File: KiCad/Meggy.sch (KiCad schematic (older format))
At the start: 2 parts, among them U1 ROM-42pin, U2 AT90USB1286-MU

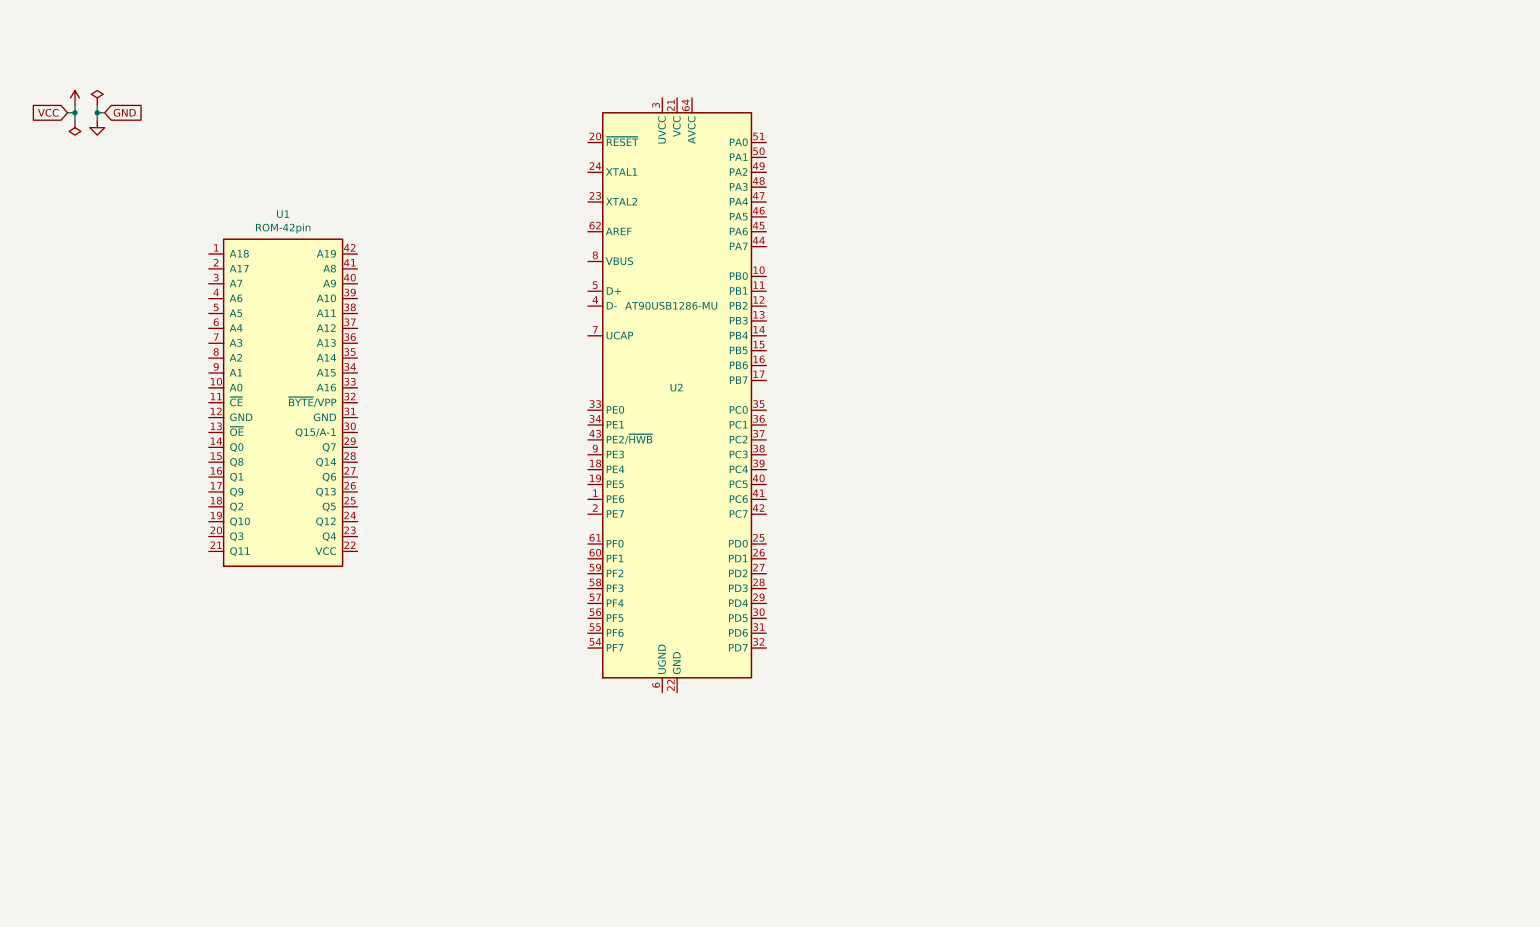
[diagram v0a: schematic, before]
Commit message: Add Micro USB connector and resistors R1-R3
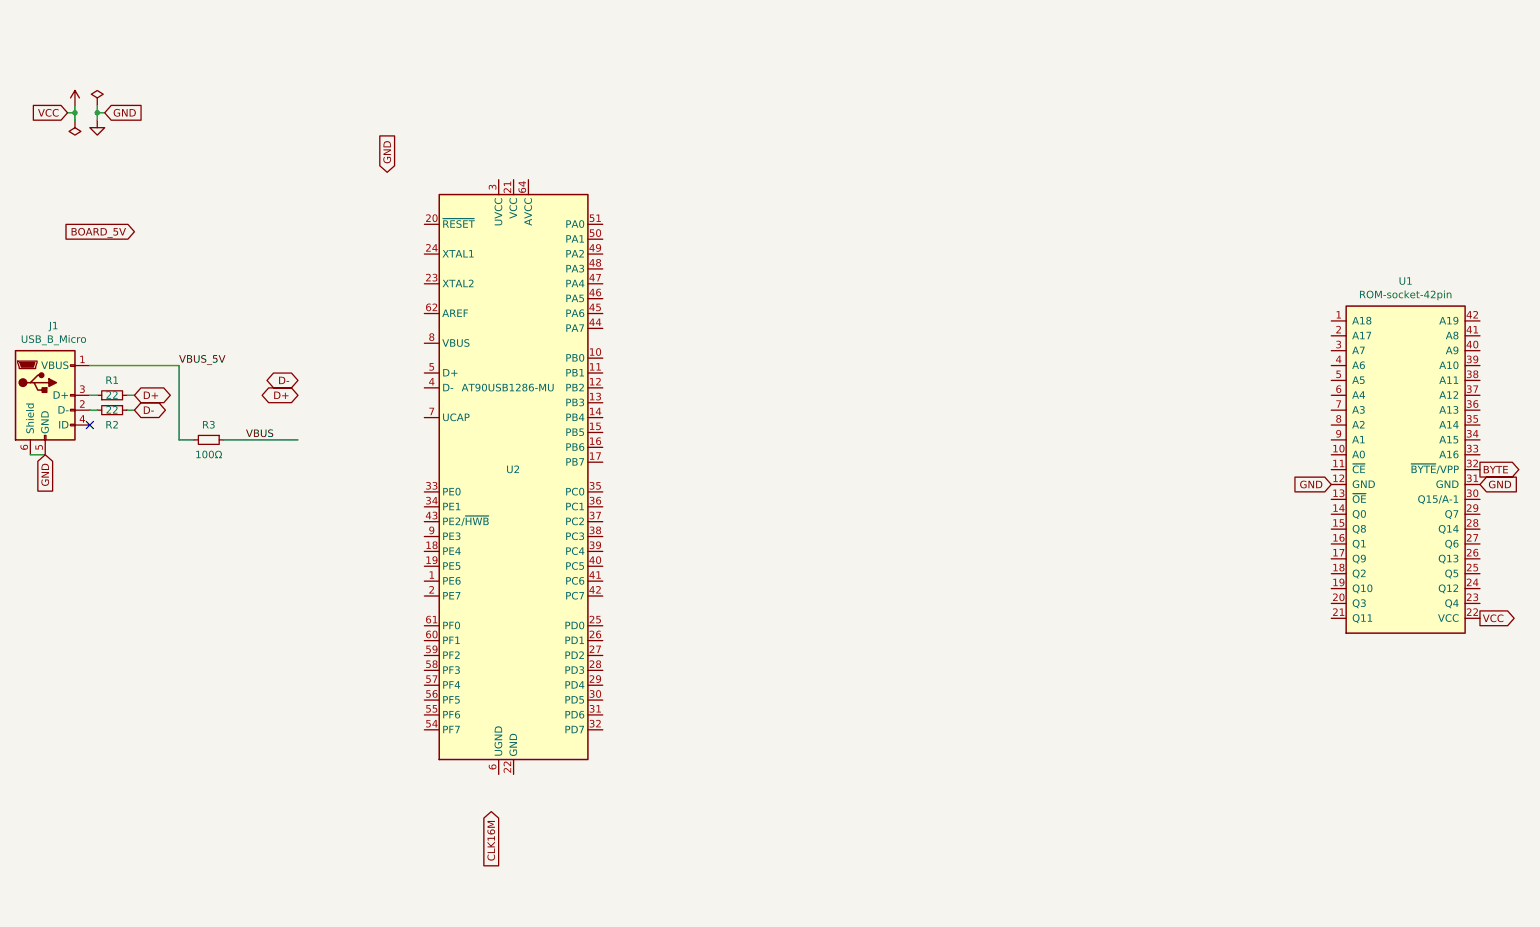
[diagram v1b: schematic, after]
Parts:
- added J1: USB_B_Micro, Meggy:101181940001LF, symbol Connector:USB_B_Micro
- added R1, R2: 22, Resistor_SMD:R_0603_1608Metric_Pad0.98x0.95mm_HandSolder, symbol Device:R_Small
- added R3: 100Ω, Resistor_SMD:R_0603_1608Metric_Pad0.98x0.95mm_HandSolder, symbol Device:R_Small
- U1: value ROM-42pin -> ROM-socket-42pin
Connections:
- net labels added: BOARD_5V, BYTE, CLK16M, D+, D-, VBUS, VBUS_5V
- wire segments 6 -> 15
- no-connect marks 0 -> 1
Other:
- moved on the sheet: U1, U2
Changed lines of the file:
@@
 	1200 1150 1200 1200
+$Comp
+L Meggy:AT90USB1286-MU U2
+U 1 1 68CAE842
+P 4000 3600
+F 0 "U2" H 3950 3650 50  0000 L CNN
+F 1 "AT90USB1286-MU" H 3650 4200 50  0000 L CNN
+F 2 "Meggy:QFN50P900X900X100-65N-D" H 5200 5450 50  0001 L CNN
+F 3 "" H 5200 5350 50  0001 L CNN
+	1    4000 3600
+	1    0    0    -1
+$EndComp
+Text GLabel 1450 3150 2    50   BiDi ~ 0
+D-
+Text GLabel 1450 3050 2    50   BiDi ~ 0
+D+
+Text GLabel 3850 5850 3    50   Input ~ 0
+CLK16M
+Text GLabel 850  3450 3    50   Input ~ 0
+GND
+$Comp
+L Connector:USB_B_Micro J1
+U 1 1 68CB996A
+P 850 3050
+F 0 "J1" H 907 3517 50  0000 C CNN
+F 1 "USB_B_Micro" H 907 3426 50  0000 C CNN
+F 2 "Meggy:101181940001LF" H 1000 3000 50  0001 C CNN
+F 3 "~" H 1000 3000 50  0001 C CNN
+	1    850  3050
+	1    0    0    -1
+$EndComp
 $Comp
 L Meggy:ROM-42pin U1
 U 1 1 68C9F45B
-P 2450 3050
-F 0 "U1" H 2450 4267 50  0000 C CNN
-F 1 "ROM-42pin" H 2450 4176 50  0000 C CNN
-F 2 "Package_DIP:DIP-42_W15.24mm" H 1900 1800 50  0001 L CNN
-F 3 "" H 2450 2800 50  0001 C CNN
-	1    2450 3050
+P 10000 3500
+F 0 "U1" H 10000 4717 50  0000 C CNN
+F 1 "ROM-socket-42pin" H 10000 4626 50  0000 C CNN
+F 2 "Package_DIP:DIP-42_W15.24mm" H 9450 2250 50  0001 L CNN
+F 3 "" H 10000 3250 50  0001 C CNN
+	1    10000 3500
 	1    0    0    -1
 $EndComp
+Text Label 1750 2850 0    50   ~ 0
+VBUS_5V
+Text Label 2200 3350 0    50   ~ 0
+VBUS
 $Comp
-L Meggy:AT90USB1286-MU U2
-U 1 1 68CAE842
-P 5100 3050
-F 0 "U2" H 5050 3100 50  0000 L CNN
-F 1 "AT90USB1286-MU" H 4750 3650 50  0000 L CNN
-F 2 "Meggy:QFN50P900X900X100-65N-D" H 6300 4900 50  0001 L CNN
-F 3 "" H 6300 4800 50  0001 L CNN
-	1    5100 3050
-	1    0    0    -1
+L Device:R_Small R2
+U 1 1 68CDBA06
+P 1300 3150
+F 0 "R2" V 1400 3150 50  0000 C CNN
+F 1 "22" V 1300 3150 50  0000 C CNN
+F 2 "Resistor_SMD:R_0603_1608Metric_Pad0.98x0.95mm_HandSolder" H 1300 3150 50  0001 C CNN
+F 3 "~" H 1300 3150 50  0001 C CNN
+	1    1300 3150
+	0    1    1    0
 $EndComp
+$Comp
+L Device:R_Small R1
+U 1 1 68CCF898
+P 1300 3050
+F 0 "R1" V 1400 3050 50  0000 C CNN
+F 1 "22" V 1300 3050 50  0000 C CNN
+F 2 "Resistor_SMD:R_0603_1608Metric_Pad0.98x0.95mm_HandSolder" H 1300 3050 50  0001 C CNN
+F 3 "~" H 1300 3050 50  0001 C CNN
+	1    1300 3050
+	0    -1   -1   0
+$EndComp
+Wire Wire Line
+	1150 3050 1200 3050
+Wire Wire Line
+	1150 3150 1200 3150
+Wire Wire Line
+	1450 3050 1400 3050
+Wire Wire Line
+	1450 3150 1400 3150
+Text GLabel 2550 3050 0    50   BiDi ~ 0
+D+
+Text GLabel 2550 2950 0    50   BiDi ~ 0
+D-
+$Comp
+L Device:R_Small R3
+U 1 1 68CDBE7C
+P 1950 3350
+F 0 "R3" V 1850 3350 50  0000 C CNN
+F 1 "100Ω" V 2050 3350 50  0000 C CNN
+F 2 "Resistor_SMD:R_0603_1608Metric_Pad0.98x0.95mm_HandSolder" H 1950 3350 50  0001 C CNN
+F 3 "~" H 1950 3350 50  0001 C CNN
+	1    1950 3350
+	0    1    1    0
+$EndComp
+Wire Wire Line
+	1150 2850 1750 2850
+Wire Wire Line
+	1750 2850 1750 3350
+Wire Wire Line
+	1750 3350 1850 3350
+Wire Wire Line
+	2050 3350 2550 3350
+NoConn ~ 1150 3250
+Wire Wire Line
+	750  3450 850  3450
+Text GLabel 1450 1950 0    50   Input ~ 0
+BOARD_5V
+Text GLabel 10500 4550 2    50   Output ~ 0
+VCC
+Text GLabel 9500 3650 0    50   Input ~ 0
+GND
+Text GLabel 10500 3650 2    50   Input ~ 0
+GND
+Text GLabel 10500 3550 2    50   Output ~ 0
+BYTE
+Text GLabel 3150 1550 1    50   Input ~ 0
+GND
 $EndSCHEMATC

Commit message: Add U3 M29F160F, pin assignment and preliminary routing
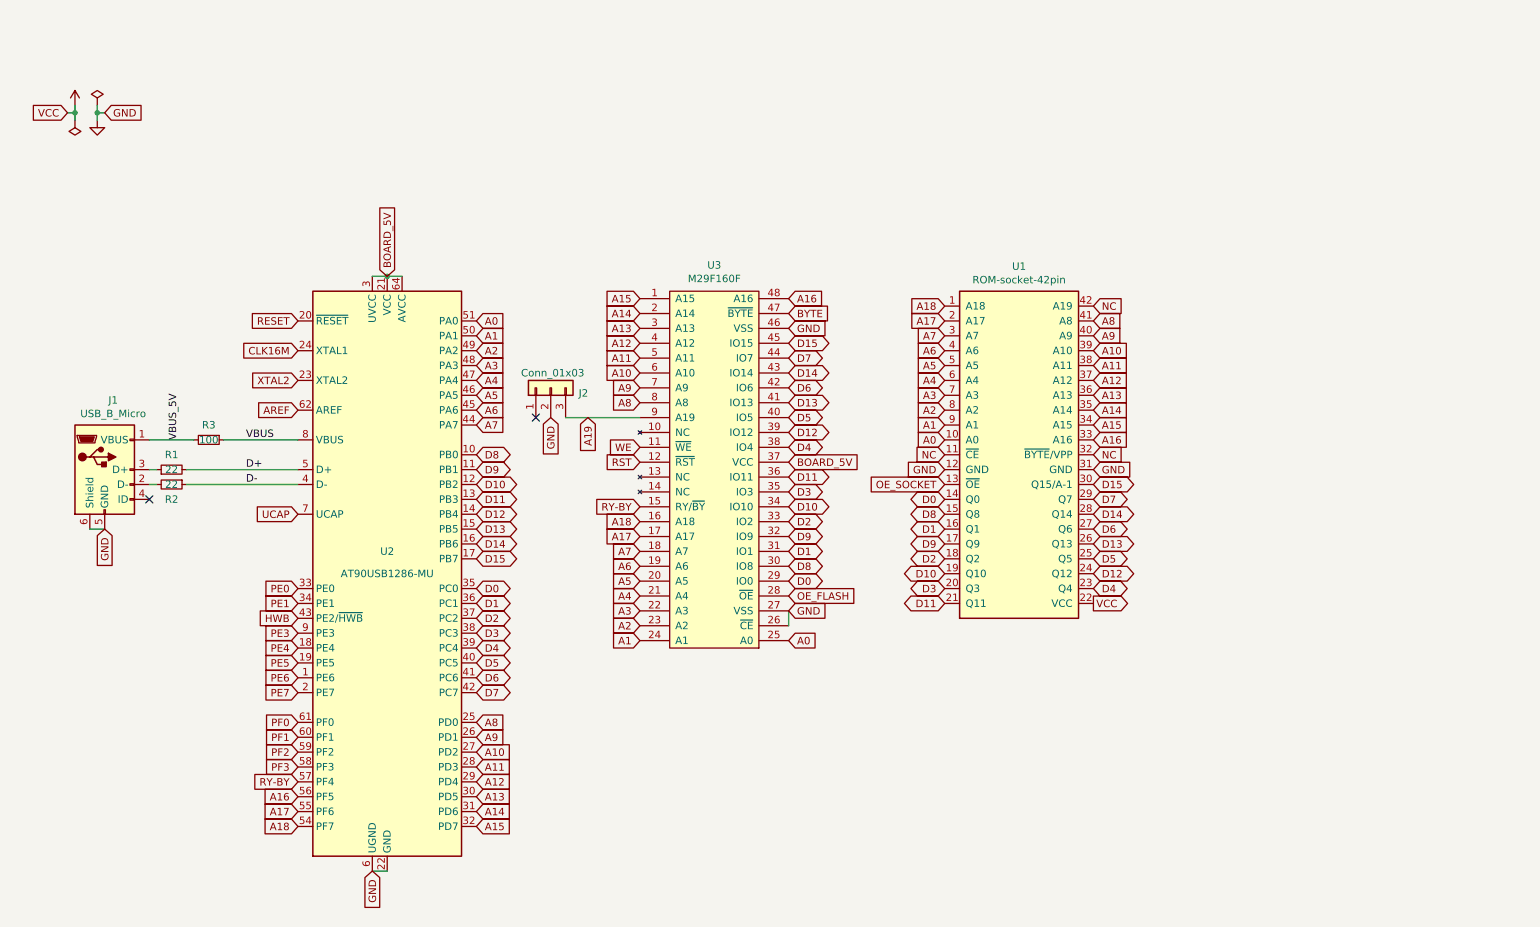
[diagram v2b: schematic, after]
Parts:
- removed U2: AT90USB1286-MU, Meggy:QFN50P900X900X100-65N-D, symbol Meggy:AT90USB1286-MU
- added J2: Conn_01x03, Connector_PinHeader_2.54mm:PinHeader_1x03_P2.54mm_Vertical, symbol Connector_Generic:Conn_01x03
- added U2: AT90USB1286-MU, Meggy:QFN50P900X900X100-65N-D, symbol MCU_Microchip_AVR:AT90USB1286-MU
- added U3: M29F160F, Package_SO:TSOP-I-48_18.4x12mm_P0.5mm, symbol Meggy:M29F160F
- R3: value 100Ω -> 100
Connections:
- net labels added: A0, A1, A10, A11, A12, A13, A14, A15, A16, A17, A18, A19, A2, A3, A4, A5, A6, A7, A8, A9, AREF, D0, D1, D10, D11, D12, D13, D14, D15, D2, D3, D4, D5, D6, D7, D8, D9, HWB, NC, OE_FLASH, OE_SOCKET, PE0, PE1, PE3, PE4, PE5, PE6, PE7, PF0, PF1, PF2, PF3, RESET, RST, RY-BY, UCAP, WE, XTAL2
- wire segments 15 -> 18
- no-connect marks 1 -> 2
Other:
- moved on the sheet: J1, R1, R2, U1

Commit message: Add capacitors and a XTAL_OSC plus 22 Ohm resistor for 16MHz clock and more placement and routing
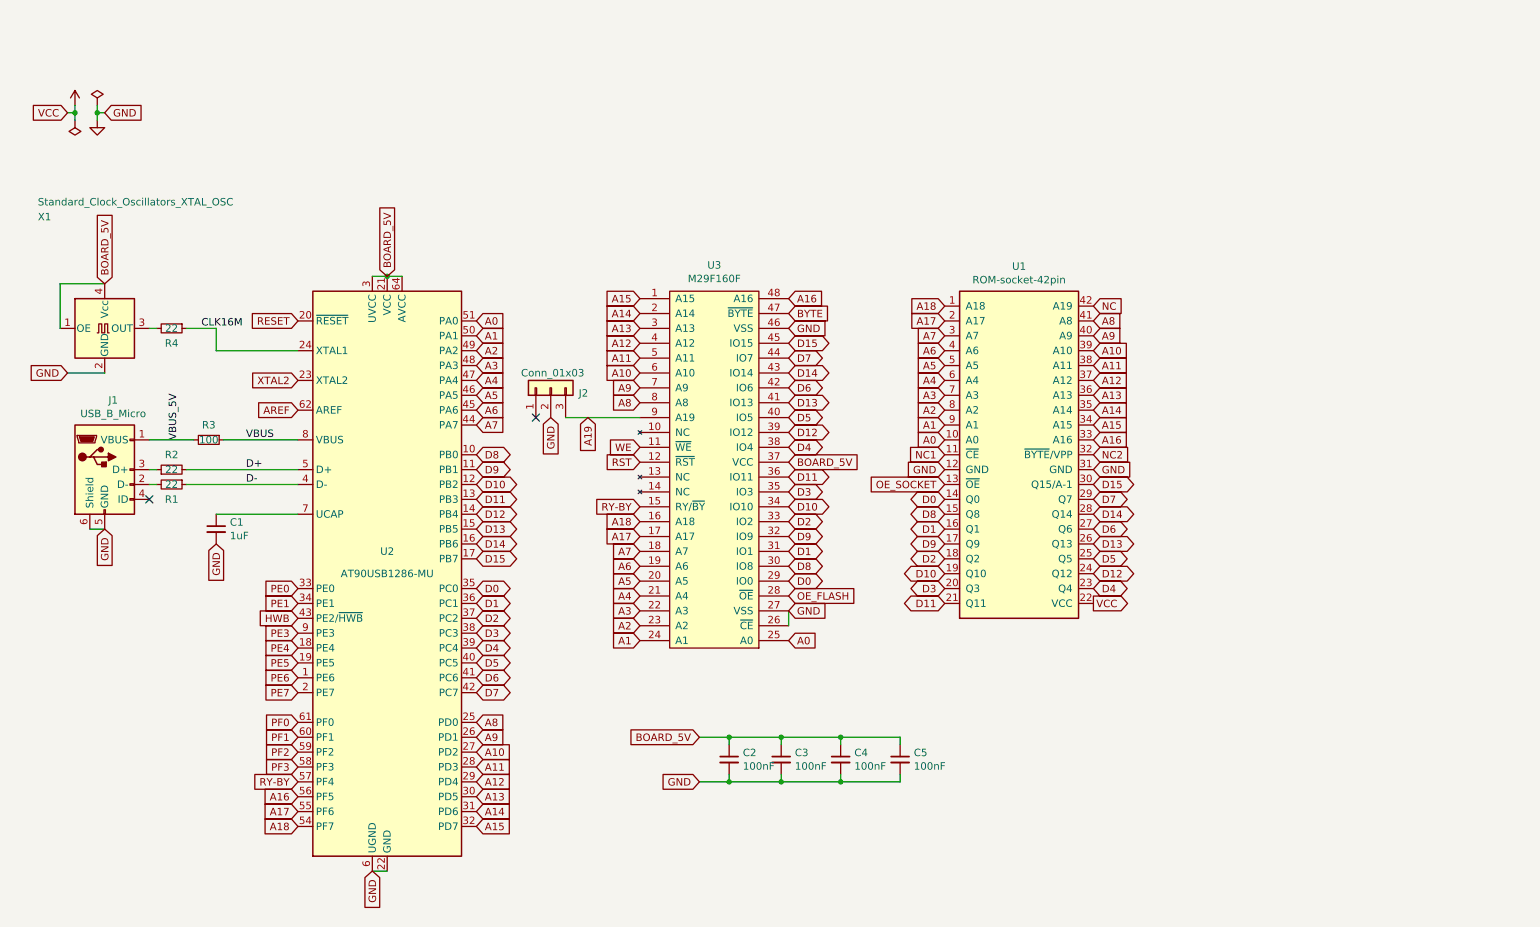
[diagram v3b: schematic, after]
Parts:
- added C1: 1uF, Capacitor_SMD:C_0603_1608Metric_Pad1.08x0.95mm_HandSolder, symbol Device:C_Small
- added C2, C3, C4, C5: 100nF, Capacitor_SMD:C_0603_1608Metric_Pad1.08x0.95mm_HandSolder, symbol Device:C_Small
- added R4: 22, Resistor_SMD:R_0603_1608Metric_Pad0.98x0.95mm_HandSolder, symbol Device:R_Small
- added X1: Standard_Clock_Oscillators_XTAL_OSC, Oscillator:Oscillator_SMD_SeikoEpson_SG8002LB-4Pin_5.0x3.2mm, symbol Oscillator:Standard_Clock_Oscillators_XTAL_OSC
- renumbered R2 to R1, R1 to R2
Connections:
- net BOARD_5V: now also C2.1, C3.1, C4.1, C5.1, X1.1 (OE), X1.4 (Vcc)
- net CLK16M: now also R4.1
- net GND: now also C1.2, C2.2, C3.2, C4.2, C5.2, X1.2 (GND)
- net NC: no longer U1.11 (~CE), U1.32 (~BYTE~/VPP)
- net UCAP: no longer names the net of U2.7 (UCAP)
- net UCAP: now also C1.1
- new net: R4.2, X1.3 (OUT)
- new net NC1: U1.11 (~CE)
- new net NC2: U1.32 (~BYTE~/VPP)
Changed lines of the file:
@@
 Wire Wire Line
 	1200 1150 1200 1200
-Text GLabel 2550 2750 0    50   Input ~ 0
-CLK16M
 Text GLabel 1250 3950 3    50   Input ~ 0
 GND
@@
 VBUS
 $Comp
-L Device:R_Small R2
+L Device:R_Small R1
 U 1 1 68CDBA06
 P 1700 3650
-F 0 "R2" V 1800 3650 50  0000 C CNN
+F 0 "R1" V 1800 3650 50  0000 C CNN
 F 1 "22" V 1700 3650 50  0000 C CNN
 F 2 "Resistor_SMD:R_0603_1608Metric_Pad0.98x0.95mm_HandSolder" H 1700 3650 50  0001 C CNN
@@
 GND
 Text GLabel 7900 3450 2    50   Input ~ 0
-NC
+NC2
 Text GLabel 3050 6250 3    50   Input ~ 0
 GND
@@
 D-
 $Comp
-L Device:R_Small R1
+L Device:R_Small R2
 U 1 1 68CCF898
 P 1700 3550
-F 0 "R1" V 1800 3550 50  0000 C CNN
+F 0 "R2" V 1800 3550 50  0000 C CNN
 F 1 "22" V 1700 3550 50  0000 C CNN
 F 2 "Resistor_SMD:R_0603_1608Metric_Pad0.98x0.95mm_HandSolder" H 1700 3550 50  0001 C CNN
@@
 D15
 Text GLabel 6900 3450 0    50   Input ~ 0
-NC
+NC1
 Wire Wire Line
 	5850 4500 5850 4600
@@
 Text GLabel 2550 3150 0    50   Input ~ 0
 AREF
-Text GLabel 2550 3850 0    50   Input ~ 0
-UCAP
 Text GLabel 2550 4550 0    50   Input ~ 0
 HWB
@@
 Text GLabel 2550 5850 0    50   Input ~ 0
 A17
+$Comp
+L Oscillator:Standard_Clock_Oscillators_XTAL_OSC X1
+U 1 1 68CF909B
+P 1250 2600
+F 0 "X1" H 800 3350 50  0000 L CNN
+F 1 "Standard_Clock_Oscillators_XTAL_OSC" H 800 3450 50  0000 L CNN
+F 2 "Oscillator:Oscillator_SMD_SeikoEpson_SG8002LB-4Pin_5.0x3.2mm" H 1950 2250 50  0001 C CNN
+F 3 "" H 1150 2600 50  0001 C CNN
+	1    1250 2600
+	1    0    0    -1
+$EndComp
+Text GLabel 1250 2300 1    50   Input ~ 0
+BOARD_5V
+Wire Wire Line
+	950  2600 950  2300
+Wire Wire Line
+	950  2300 1250 2300
+Text GLabel 1000 2900 0    50   Input ~ 0
+GND
+Wire Wire Line
+	1000 2900 1250 2900
+$Comp
+L Device:R_Small R4
+U 1 1 68CFCC9A
+P 1700 2600
+F 0 "R4" V 1800 2600 50  0000 C CNN
+F 1 "22" V 1700 2600 50  0000 C CNN
+F 2 "Resistor_SMD:R_0603_1608Metric_Pad0.98x0.95mm_HandSolder" H 1700 2600 50  0001 C CNN
+F 3 "~" H 1700 2600 50  0001 C CNN
+	1    1700 2600
+	0    1    1    0
+$EndComp
+Wire Wire Line
+	1550 2600 1600 2600
+Wire Wire Line
+	1800 2600 2000 2600
+Wire Wire Line
+	2000 2600 2000 2750
+Wire Wire Line
+	2000 2750 2550 2750
+Text Label 1900 2600 0    50   ~ 0
+CLK16M
+$Comp
+L Device:C_Small C5
+U 1 1 68D04809
+P 6600 5500
+F 0 "C5" H 6692 5546 50  0000 L CNN
+F 1 "100nF" H 6692 5455 50  0000 L CNN
+F 2 "Capacitor_SMD:C_0603_1608Metric_Pad1.08x0.95mm_HandSolder" H 6600 5500 50  0001 C CNN
+F 3 "~" H 6600 5500 50  0001 C CNN
+	1    6600 5500
+	1    0    0    -1
+$EndComp
+Text GLabel 5250 5350 0    50   Input ~ 0
+BOARD_5V
+Text GLabel 5250 5650 0    50   Input ~ 0
+GND
+Wire Wire Line
+	5250 5350 5450 5350
+Wire Wire Line
+	5450 5350 5450 5400
+Wire Wire Line
+	5250 5650 5450 5650
+Wire Wire Line
+	5450 5650 5450 5600
+$Comp
+L Device:C_Small C1
+U 1 1 68D080F7
+P 2000 3950
+F 0 "C1" H 2092 3996 50  0000 L CNN
+F 1 "1uF" H 2092 3905 50  0000 L CNN
+F 2 "Capacitor_SMD:C_0603_1608Metric_Pad1.08x0.95mm_HandSolder" H 2000 3950 50  0001 C CNN
+F 3 "~" H 2000 3950 50  0001 C CNN
+	1    2000 3950
+	1    0    0    -1
+$EndComp
+Text GLabel 2000 4050 3    50   Input ~ 0
+GND
+Wire Wire Line
+	2550 3850 2000 3850
+$Comp
+L Device:C_Small C2
+U 1 1 68D18519
+P 5450 5500
+F 0 "C2" H 5542 5546 50  0000 L CNN
+F 1 "100nF" H 5542 5455 50  0000 L CNN
+F 2 "Capacitor_SMD:C_0603_1608Metric_Pad1.08x0.95mm_HandSolder" H 5450 5500 50  0001 C CNN
+F 3 "~" H 5450 5500 50  0001 C CNN
+	1    5450 5500
+	1    0    0    -1
+$EndComp
+$Comp
+L Device:C_Small C3
+U 1 1 68D18C10
+P 5800 5500
+F 0 "C3" H 5892 5546 50  0000 L CNN
+F 1 "100nF" H 5892 5455 50  0000 L CNN
+F 2 "Capacitor_SMD:C_0603_1608Metric_Pad1.08x0.95mm_HandSolder" H 5800 5500 50  0001 C CNN
+F 3 "~" H 5800 5500 50  0001 C CNN
+	1    5800 5500
+	1    0    0    -1
+$EndComp
+Wire Wire Line
+	5800 5400 5800 5350
+Wire Wire Line
+	5800 5350 5450 5350
+Connection ~ 5450 5350
+Wire Wire Line
+	6200 5400 6200 5350
+Wire Wire Line
+	6200 5350 5800 5350
+Connection ~ 5800 5350
+Wire Wire Line
+	5450 5650 5800 5650
+Wire Wire Line
+	5800 5650 5800 5600
+Connection ~ 5450 5650
+Wire Wire Line
+	5800 5650 6200 5650
+Wire Wire Line
+	6200 5650 6200 5600
+Connection ~ 5800 5650
+$Comp
+L Device:C_Small C4
+U 1 1 68D246B1
+P 6200 5500
+F 0 "C4" H 6292 5546 50  0000 L CNN
+F 1 "100nF" H 6292 5455 50  0000 L CNN
+F 2 "Capacitor_SMD:C_0603_1608Metric_Pad1.08x0.95mm_HandSolder" H 6200 5500 50  0001 C CNN
+F 3 "~" H 6200 5500 50  0001 C CNN
+	1    6200 5500
+	1    0    0    -1
+$EndComp
+Wire Wire Line
+	6200 5350 6600 5350
+Wire Wire Line
+	6600 5350 6600 5400
+Connection ~ 6200 5350
+Wire Wire Line
+	6200 5650 6600 5650
+Wire Wire Line
+	6600 5650 6600 5600
+Connection ~ 6200 5650
 $EndSCHEMATC
